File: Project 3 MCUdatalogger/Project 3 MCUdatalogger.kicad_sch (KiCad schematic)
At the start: 25 parts, among them U1 24LC1025, U2 DS1337S_, U3 24LC1025, U4 ATMEGA328P-AU, Y1 32.768 KHz, Y2 16 MHz

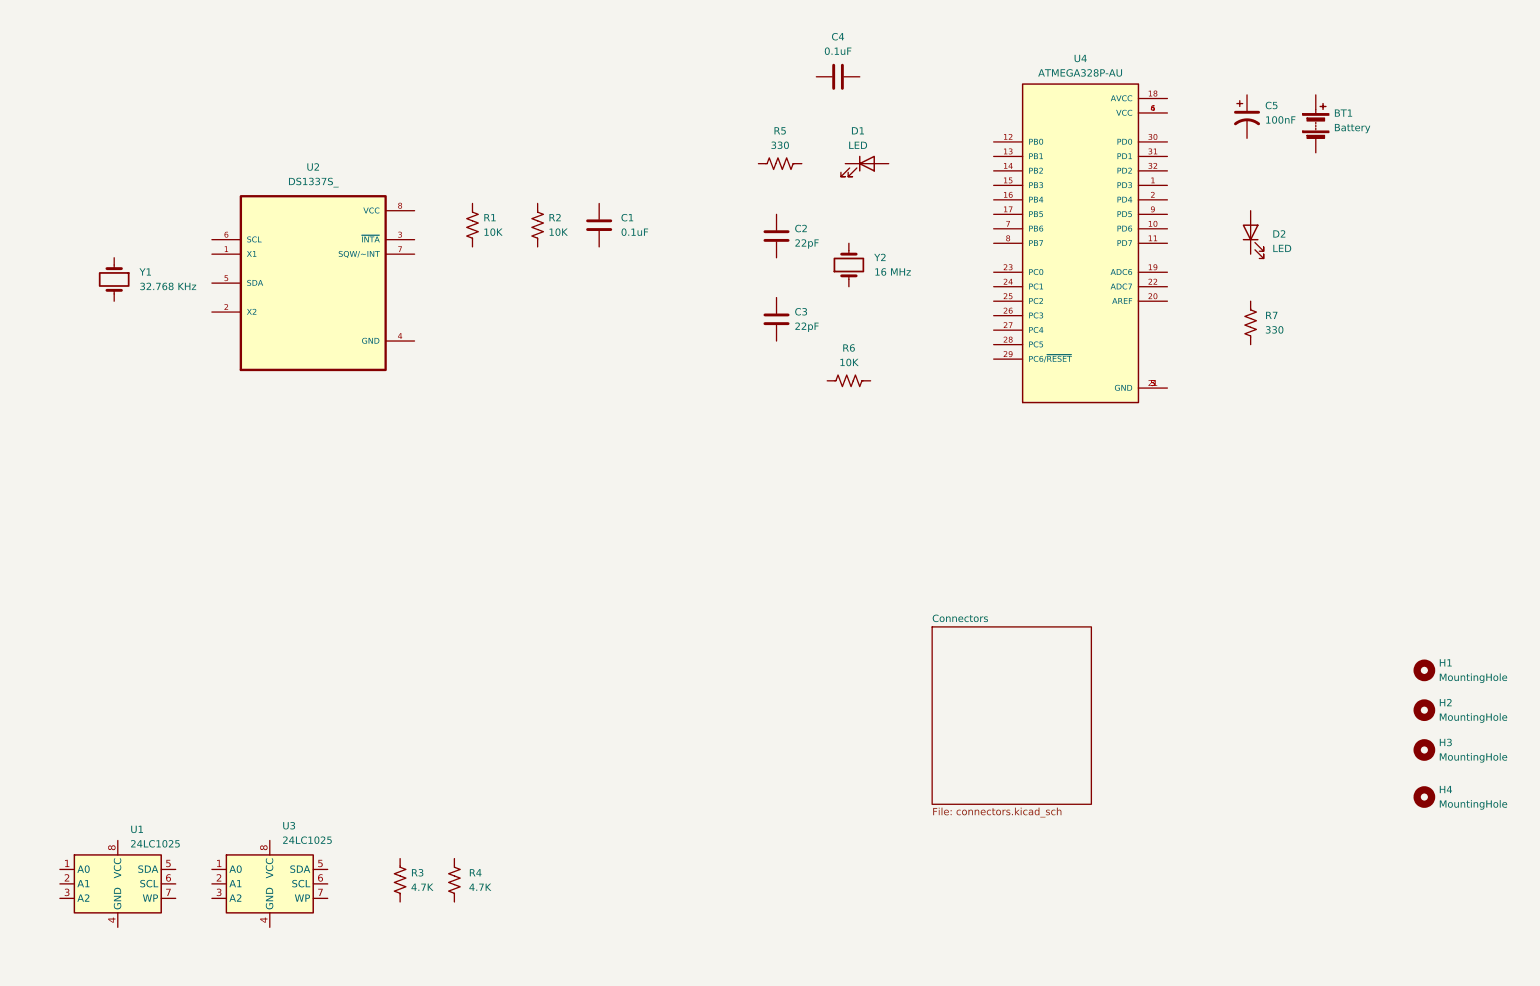
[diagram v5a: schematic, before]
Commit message: Completed wiring of main sheet.
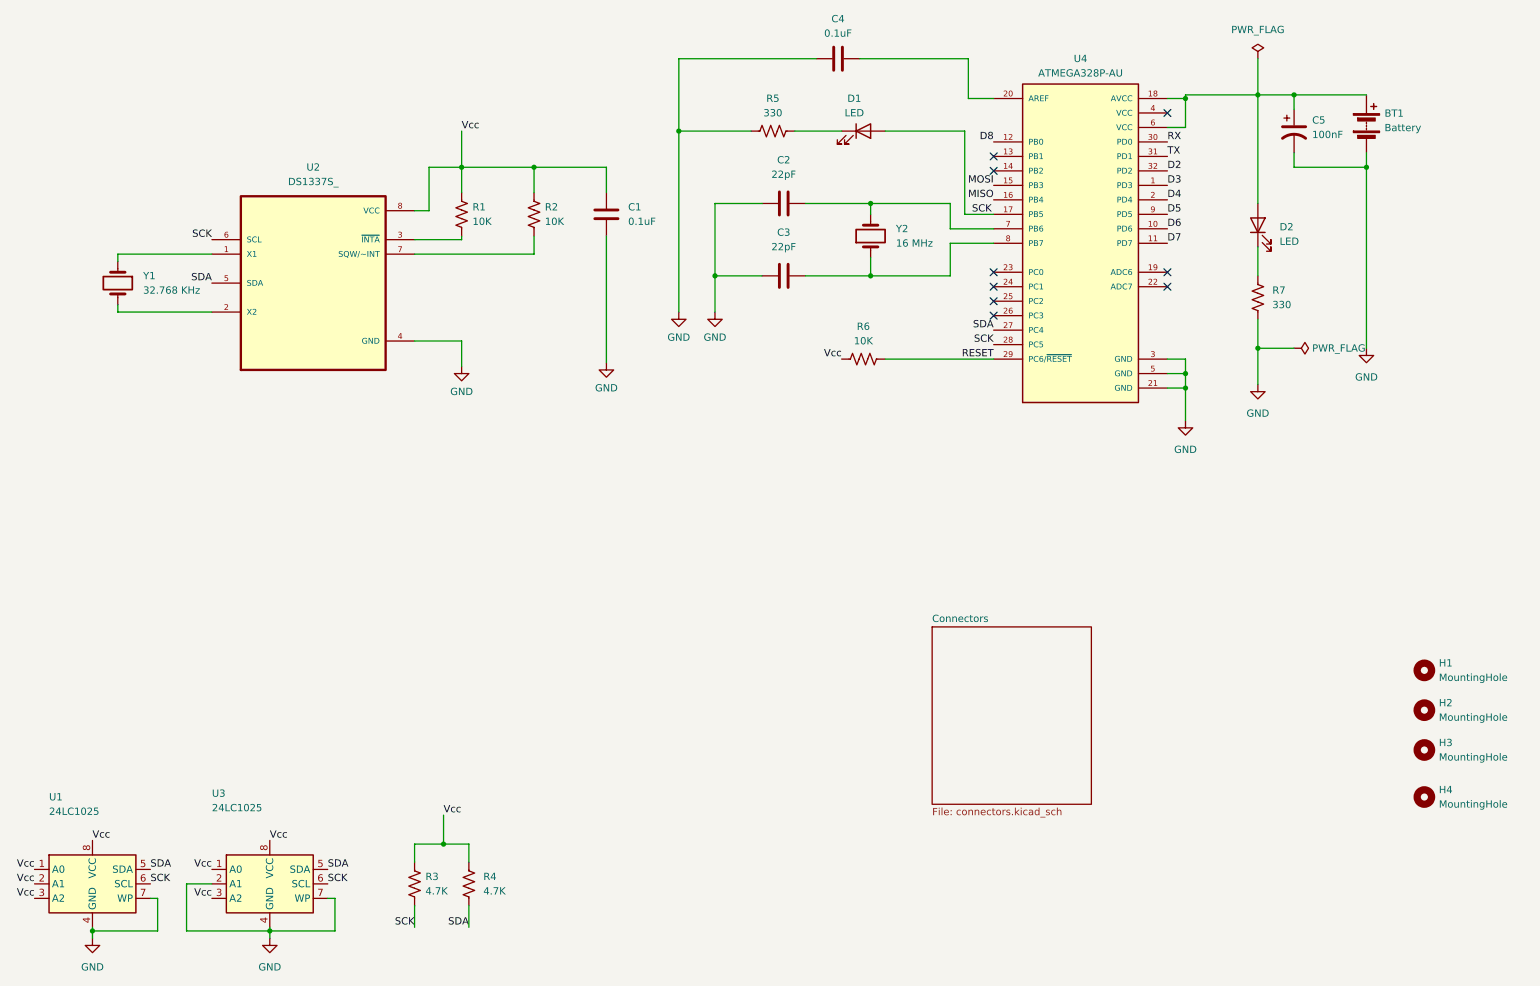
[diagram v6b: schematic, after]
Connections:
- net at C5.1: now also BT1.1 (+), D2.2 (A), U4.18 (AVCC), U4.6 (VCC)
- net GND: now reaches C5.2
- net GND: now also BT1.2 (-), C1.2, C2.1, C3.1, C4.1, R5.1, R7.2, U1.4 (GND), U1.7 (WP), U2.4 (GND), U3.2 (A1), U3.4 (GND), U3.7 (WP), U4.21 (GND), U4.3 (GND), U4.5 (GND)
- net at D1.1 (K): now also R5.2
- net SCK: now reaches D1.2 (A)
- net SCK: now also R3.2, U1.6 (SCL), U2.6 (SCL), U3.6 (SCL), U4.17 (PB5), U4.28 (PC5)
- net at C3.2: now also U4.8 (PB7), Y2.1
- net Vcc: now reaches R1.1
- net Vcc: now also C1.1, R2.1, R3.1, R4.1, R6.1, U1.1 (A0), U1.2 (A1), U1.3 (A2), U1.8 (VCC), U2.8 (VCC), U3.1 (A0), U3.3 (A2), U3.8 (VCC)
- net at R1.2: now also U2.3 (~{INTA})
- net at D2.1 (K): now also R7.1
- net at C4.2: now also U4.20 (AREF)
- net at Y2.2: now also C2.2, U4.7 (PB6)
- net D3: now reaches U4.1 (PD3)
- net D6: now reaches U4.10 (PD6)
- net D7: now reaches U4.11 (PD7)
- net D8: now reaches U4.12 (PB0)
- net MOSI: now reaches U4.15 (PB3)
- net MISO: now reaches U4.16 (PB4)
- net D4: now reaches U4.2 (PD4)
- net SDA: now reaches U4.27 (PC4)
- net SDA: now also R4.2, U1.5 (SDA), U2.5 (SDA), U3.5 (SDA)
- net RESET: now reaches U4.29 (PC6/~{RESET})
- net RESET: now also R6.2
- net RX: now reaches U4.30 (PD0)
- net TX: now reaches U4.31 (PD1)
- net D2: now reaches U4.32 (PD2)
- net at U4.4 (VCC): no longer U4.6 (VCC)
- net D5: now reaches U4.9 (PD5)
- net at R2.2: now also U2.7 (SQW/~INT)
- net at U2.1 (X1): now also Y1.1
- net at U2.2 (X2): now also Y1.2
- no-connect marks 0 -> 9
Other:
- moved on the sheet: BT1, C1, C2, C3, C4, C5, D1, D2, R1, R2, R3, R4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

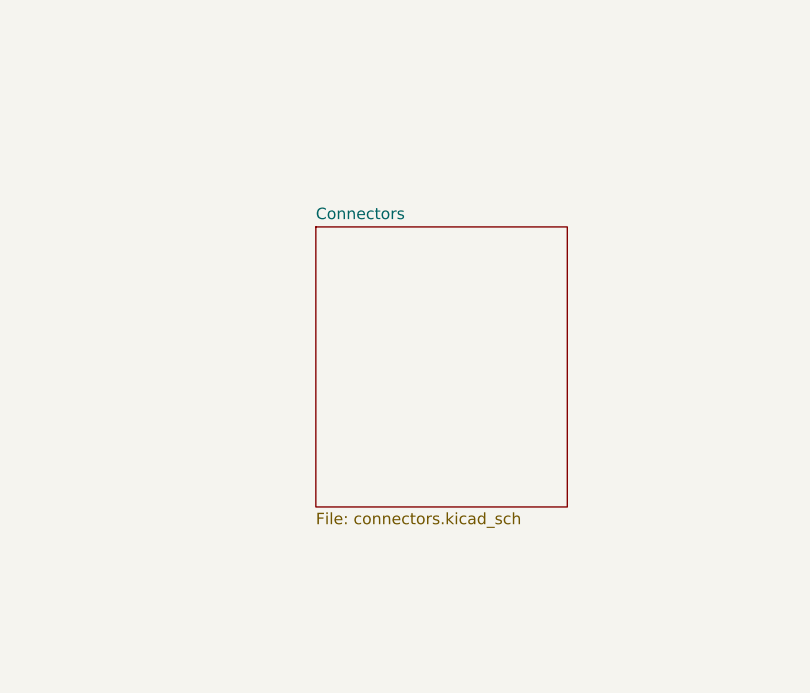
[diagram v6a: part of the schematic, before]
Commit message: Completed wiring in the second sheet.
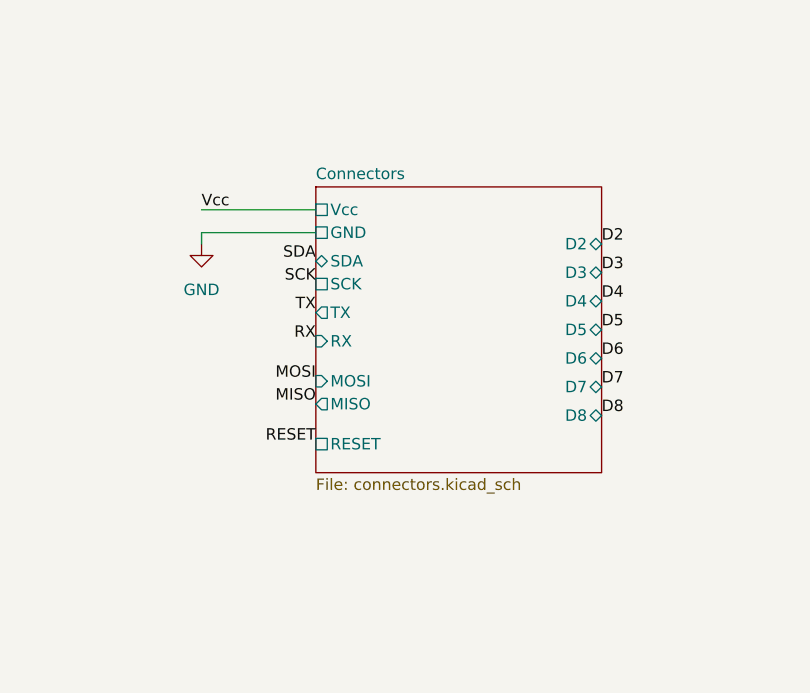
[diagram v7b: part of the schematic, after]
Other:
- sheet Connectors ports: added D2, D3, D4, D5, D6, D7, D8, GND, MISO, MOSI, RESET, RX, SCK, SDA, TX, Vcc; removed none

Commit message: Allocated GND and Vcc nets to the Power net class.
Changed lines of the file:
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@@
 	)
 	(junction
+		(at 101.6 50.8)
+		(diameter 0)
+		(color 0 0 0 0)
+	)
+	(junction
 		(at 95.25 50.8)
 		(diameter 0)
@@
 	(wire
 		(pts
+			(xy 101.6 44.45) (xy 101.6 50.8)
+		)
+		(stroke
+			(width 0)
+			(type default)
+		)
+	)
+	(wire
+		(pts
 			(xy 96.52 180.34) (xy 96.52 184.15)
 		)
@@
 	(wire
 		(pts
+			(xy 101.6 50.8) (xy 107.95 50.8)
+		)
+		(stroke
+			(width 0)
+			(type default)
+		)
+	)
+	(wire
+		(pts
 			(xy 188.595 64.135) (xy 180.975 64.135)
 		)
@@
 	(wire
 		(pts
-			(xy 95.25 50.8) (xy 107.95 50.8)
+			(xy 95.25 50.8) (xy 101.6 50.8)
 		)
 		(stroke
@@
 					(unit 1)
 				)
+			)
+		)
+	)
+	(symbol
+		(lib_id "power:PWR_FLAG")
+		(at 101.6 44.45 0)
+		(unit 1)
+		(exclude_from_sim no)
+		(in_bom yes)
+		(on_board yes)
+		(dnp no)
+		(fields_autoplaced yes)
+		(property "Reference" "#FLG03"
+			(at 101.6 42.545 0)
+			(effects
+				(font
+					(size 1.27 1.27)
+				)
+				(hide yes)
+			)
+		)
+		(property "Value" "PWR_FLAG"
+			(at 101.6 39.37 0)
+			(effects
+				(font
+					(size 1.27 1.27)
+				)
+			)
+		)
+		(property "Footprint" ""
+			(at 101.6 44.45 0)
+			(effects
+				(font
+					(size 1.27 1.27)
+				)
+				(hide yes)
+			)
+		)
+		(property "Datasheet" "~"
+			(at 101.6 44.45 0)
+			(effects
+				(font
+					(size 1.27 1.27)
+				)
+				(hide yes)
+			)
+		)
+		(property "Description" "Special symbol for telling ERC where power comes from"
+			(at 101.6 44.45 0)
+			(effects
+				(font
+					(size 1.27 1.27)
+				)
+				(hide yes)
+			)
+		)
+		(pin "1"
+		)
+		(instances
+			(project "Project 3 MCUdatalogger"
+				(path "/7d5d1e2c-b308-4025-bcdd-7450c663d83b"
+					(reference "#FLG03")
+					(unit 1)
+				)
